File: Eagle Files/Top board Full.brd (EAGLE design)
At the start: 21.8 x 20.3 mm, 19 parts

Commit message: Misc Changes
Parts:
- removed 4V, DATA, GND@1: PROTO_POINT, BLEduino Bean:1X01
- removed C1: 10uF, SparkFun-Capacitors:EIA3216
- removed J1: (no value), SparkFun-Connectors:JST-2-SMD
- added PWR1:C1: 10uF, SparkFun-Capacitors:EIA3216
- added PWR1:IC1: MCP73831/OT, adafruit:SOT23-5L
- added PWR1:J2: (no value), SparkFun-Connectors:JST-2-SMD
- added PWR1:JP1: USB-MICROB, SparkFun-Connectors:USB-MICROB
- added PWR1:R1: 470, SparkFun-Resistors:0603-RES
- added PWR1:R2: 2000, SparkFun-Resistors:0603-RES
- added R2, R3: 10K, SparkFun-Resistors:0603-RES
- added RAD1:C2: 100uF, SparkFun-Capacitors:EIA7343
- added RAD1:C3: 10pF, SparkFun-Capacitors:0603-CAP
- added RAD1:R1: 150, SparkFun-Resistors:0603-RES
- added RAD1:U$1: RD2007, radiationbean:RD2007
- moved FRAM 16.7 mm to (22.2, 11.4), turned to 90 degrees
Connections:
- removed net 4V: 4V.1
- removed net A0: FRAM.A0
- removed net A1: FRAM.A1
- removed net N$7: 0.1
- new net PWR1:N$1: PWR1:IC1.1, PWR1:R1.2
- new net PWR1:N$2: PWR1:IC1.5, PWR1:R2.2
- new net PWR1:VBUS: PWR1:C1.A, PWR1:IC1.4, PWR1:JP1.VBUS
- new net RAD1:V_SENS: RAD1:C2.A, RAD1:C3.1, RAD1:R1.2, RAD1:U$1.VCC
- net A2: now also 0.1; no longer FRAM.A2
- net CLK: now also PWR1:R1.1
- net DATA: no longer DATA.1
- net GND: now also PWR1:C1.C, PWR1:IC1.2, PWR1:J2.1, PWR1:JP1.GND, PWR1:JP1.MT1, PWR1:JP1.MT2, PWR1:R2.1, RAD1:C2.C, RAD1:C3.2, RAD1:U$1.GND; no longer C1.C, GND@1.1, J1.1
- net MOSI: now also RAD1:U$1.OUT
- net SCL: now also R3.2
- net SDA: now also R2.2
- net VBAT: now also PWR1:IC1.3, PWR1:J2.2; no longer J1.2
- net VCC: now also R2.1, R3.1, RAD1:R1.1; no longer C1.A
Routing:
- net GND: track 57.9 -> 7.59 mm
- net CLK: track 0.00 -> 22.8 mm
- net SDA: track 5.11 -> 20.8 mm
- net RAD1:V_SENS: track 0.00 -> 15.0 mm
- net DATA: track 12.7 -> 0.00 mm
- net PWR1:VBUS: track 0.00 -> 10.1 mm
- net VCC: track 14.6 -> 24.6 mm
- net SCL: track 4.46 -> 14.3 mm
- net MOSI: track 0.00 -> 8.66 mm
- net PWR1:N$1: track 0.00 -> 3.73 mm
- net PWR1:N$2: track 0.00 -> 1.76 mm
- net VBAT: track 21.3 -> 22.6 mm
- removed copper zone on layer 1, net GND
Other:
- board size 21.8 x 20.3 mm -> 45.1 x 20.3 mm
- board text added: "v0.1"
- board text removed: "Top Board"
- board text removed: "v0.2"

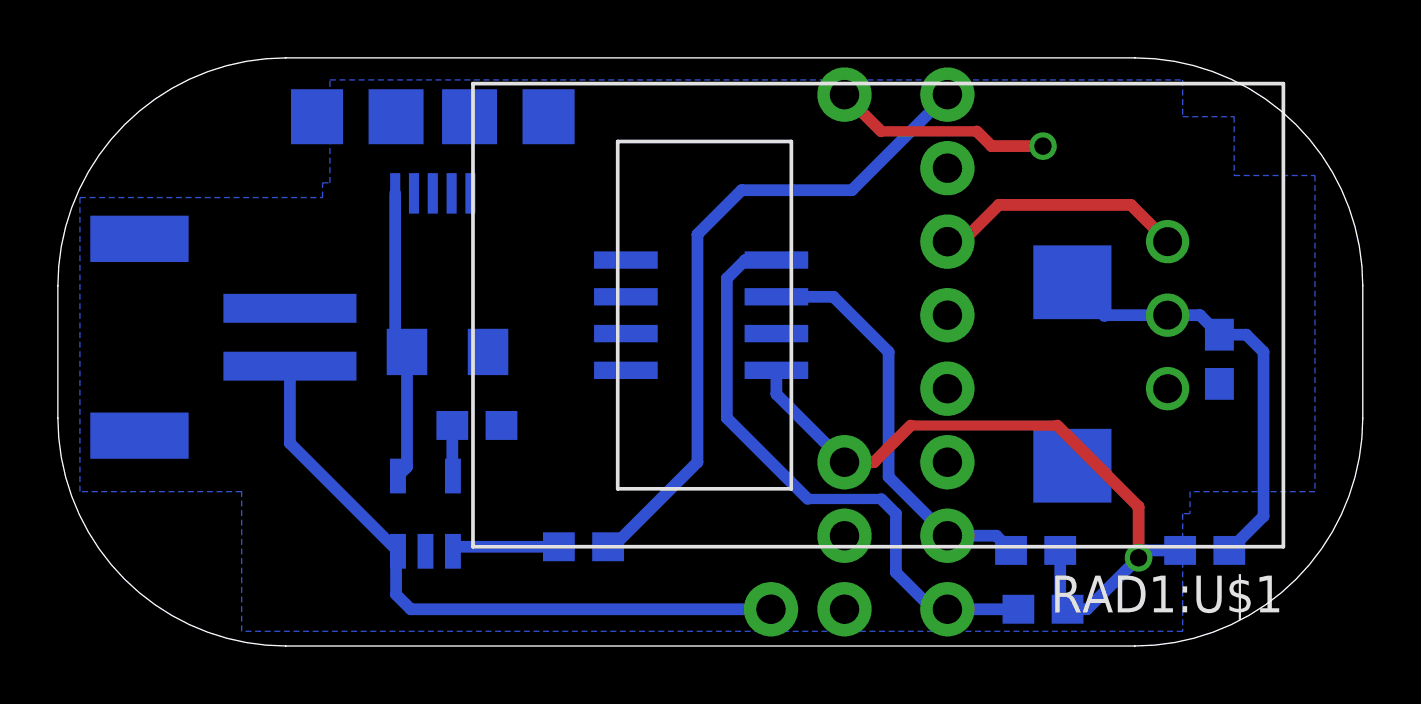
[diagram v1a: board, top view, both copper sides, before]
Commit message: Added RTC
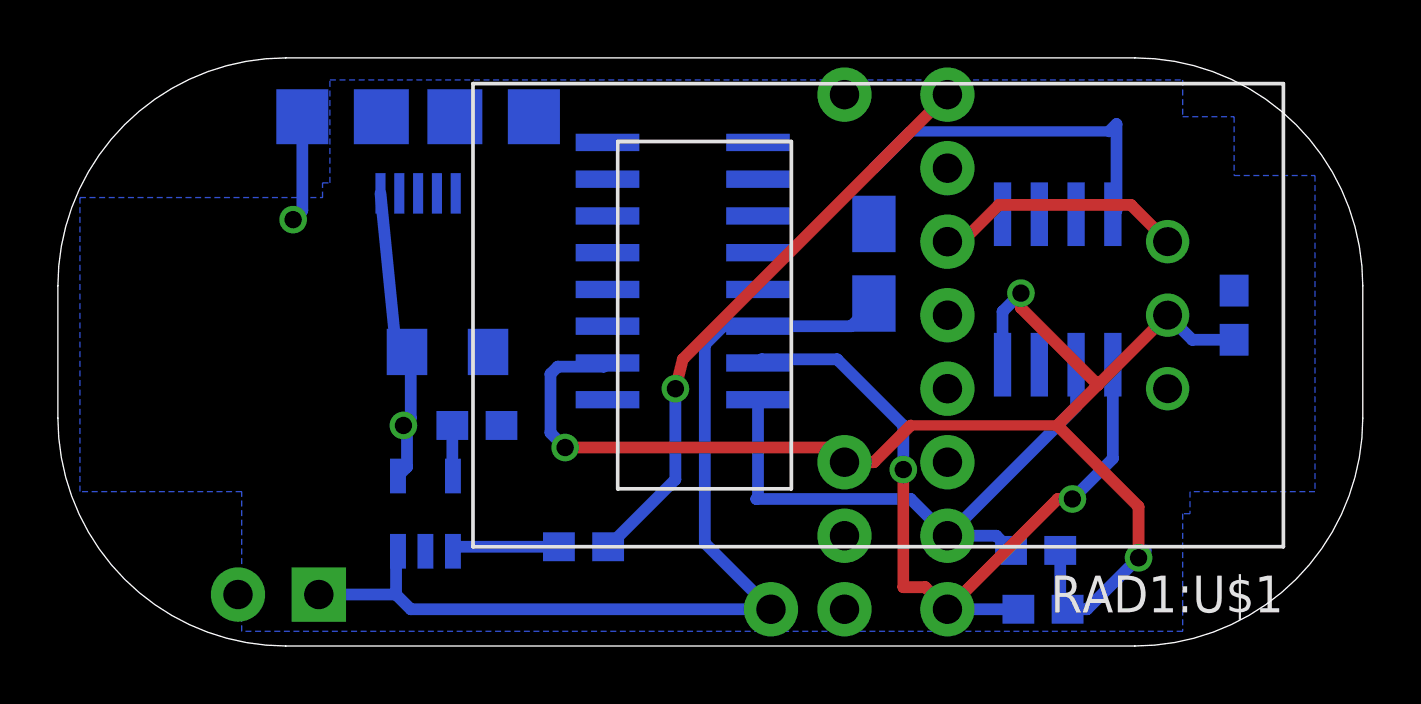
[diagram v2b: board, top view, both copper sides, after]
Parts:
- removed PWR1:J2: (no value), SparkFun-Connectors:JST-2-SMD
- removed RAD1:C2: 100uF, SparkFun-Capacitors:EIA7343
- removed RAD1:R1: 150, SparkFun-Resistors:0603-RES
- added PWR1:JP2: (no value), SparkFun-Connectors:MOLEX-1X2_LOCK
- added TIME1:C1: (no value), adafruit:A/3216-18R
- added TIME1:IC1: DS3231, radiationbean:SO16
- moved FRAM 12.4 mm to (34.5, 12.3), turned to 180 degrees
- moved RAD1:C3 1.61 mm to (40.6, 11.4)
- moved PWR1:JP1 0.51 mm to (12.4, 18.3)
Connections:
- removed net RAD1:V_SENS: RAD1:C2.A, RAD1:C3.1, RAD1:R1.2, RAD1:U$1.VCC
- net GND: now also PWR1:JP2.2, RAD1:C3.1, TIME1:C1.-, TIME1:IC1.10, TIME1:IC1.11, TIME1:IC1.12, TIME1:IC1.13, TIME1:IC1.5, TIME1:IC1.6, TIME1:IC1.7, TIME1:IC1.8, TIME1:IC1.9; no longer PWR1:J2.1, RAD1:C2.C, RAD1:C3.2
- net SCL: now also TIME1:IC1.16
- net SDA: now also TIME1:IC1.15
- net VBAT: now also PWR1:JP2.1, TIME1:C1.+, TIME1:IC1.14; no longer PWR1:J2.2
- net VCC: now also RAD1:C3.2, RAD1:U$1.VCC, TIME1:IC1.2; no longer RAD1:R1.1
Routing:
- net VCC: track 24.6 -> 49.1 mm, vias 1 -> 3
- net RAD1:V_SENS: track 15.0 -> 0.00 mm
- net VBAT: track 22.6 -> 33.9 mm
- net GND: track 7.59 -> 15.9 mm
- net SCL: track 14.3 -> 20.7 mm
- net SDA: track 20.8 -> 27.0 mm, vias 0 -> 2
- net CLK: track 22.8 -> 20.4 mm, vias 0 -> 1
- net PWR1:VBUS: track 10.1 -> 10.3 mm, vias 0 -> 1
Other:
- board text added: "Rev B"
